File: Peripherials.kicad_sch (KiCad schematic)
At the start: 32 parts, among them J12 USB_C_Receptacle_USB2.0_14P, J13 USB_C_Receptacle_USB2.0_14P, J14 IDC_Cable_02x08, J15 Conn_01x02_Pin, J18 Micro_SD_Card, Q2 NMOS, U12 USBLC6-2P6, U13 USBLC6-2P6, U2 RV-3028-C7

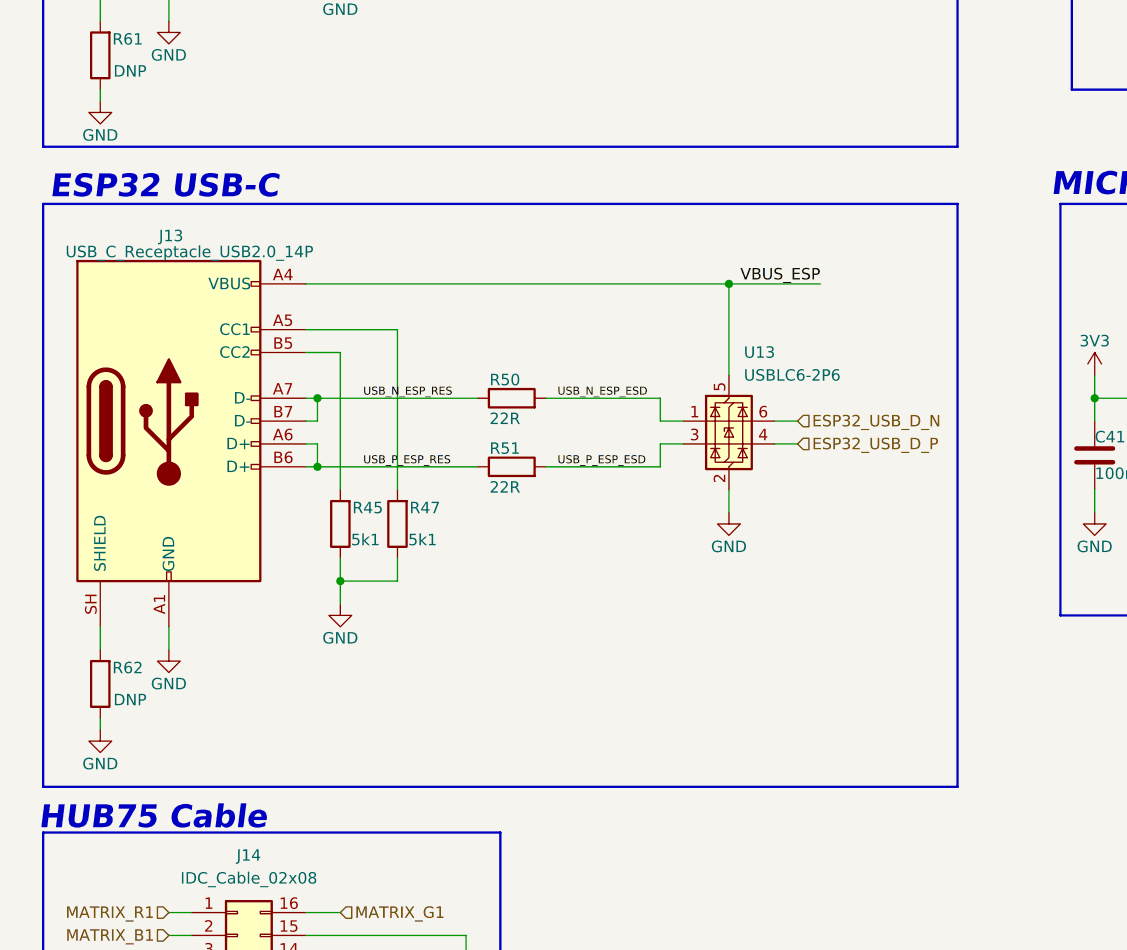
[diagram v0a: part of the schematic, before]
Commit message: got rid of usb
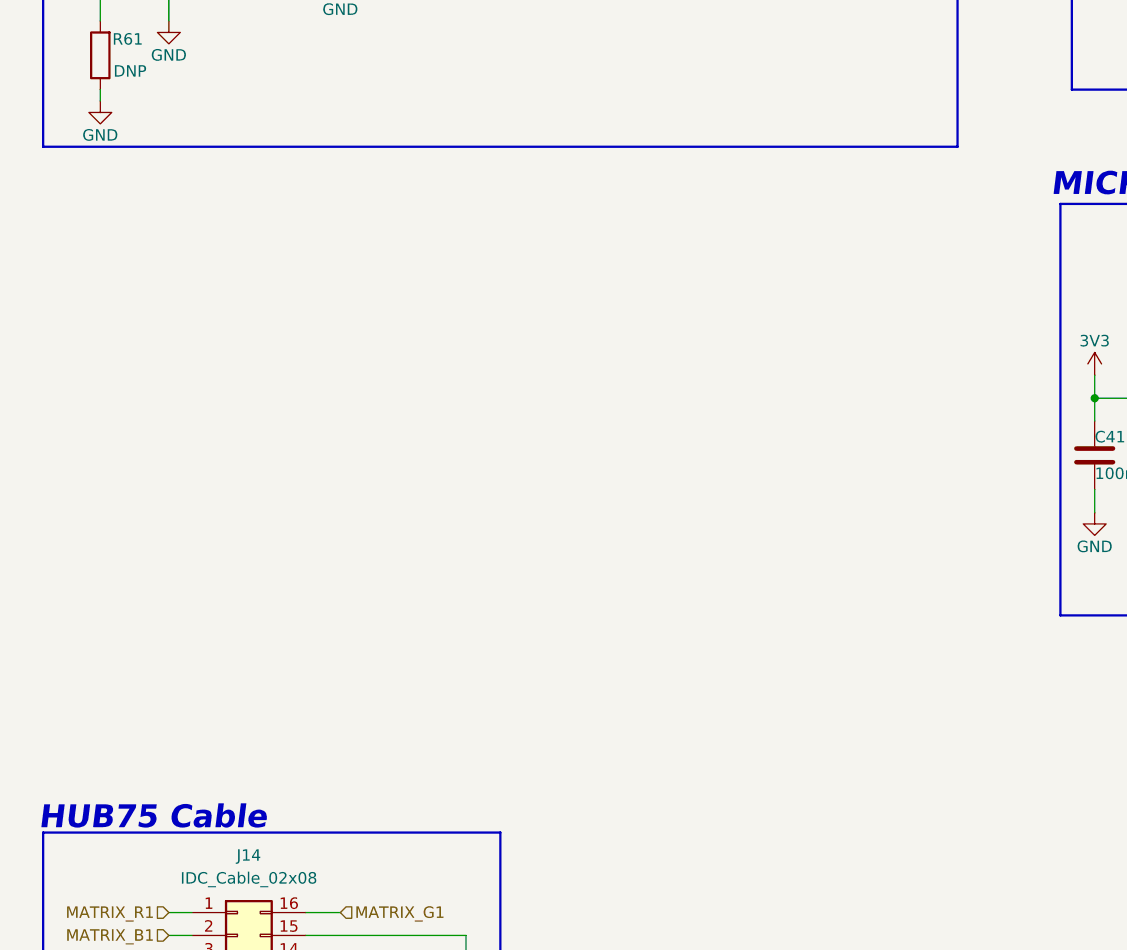
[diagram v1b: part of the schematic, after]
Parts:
- removed J13: USB_C_Receptacle_USB2.0_14P, Connector_USB:USB_C_Receptacle_Palconn_UTC16-G, symbol Connector:USB_C_Receptacle_USB2.0_14P
- removed R45, R47: 5k1, Resistor_SMD:R_0603_1608Metric, symbol Device:R
- removed R50, R51: 22R, Resistor_SMD:R_0603_1608Metric, symbol Device:R
- removed R62: DNP, Resistor_SMD:R_0603_1608Metric, symbol Device:R
- removed U13: USBLC6-2P6, Package_TO_SOT_SMD:SOT-666, symbol Power_Protection:USBLC6-2P6
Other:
- note removed: "ESP32 USB-C"

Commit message: Update Peripherials.kicad_sch
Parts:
- added J1: esp32 left side, symbol Connector_Generic:Conn_01x07
- added J2: esp32 right side, symbol Connector_Generic:Conn_01x07
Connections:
- net 3V3: now also J2.3 (Pin_3)
- net GND: now also J2.2 (Pin_2)
- net I2C3_SCL: now also J1.5 (Pin_5)
- net INT_RTC: now also J2.5 (Pin_5)
- net SPI1_MISO: now also J1.1 (Pin_1)
- net SPI1_MOSI: now also J1.2 (Pin_2)
- net SPI1_SCLK: now also J2.4 (Pin_4)
- net SPI_CS_SD_CARD: now also J1.3 (Pin_3)
- net VBUS_ESP: now also J2.1 (Pin_1)
- new net FAN_PWMD: J1.6 (Pin_6)
- new net ICC3_SDA: J1.4 (Pin_4)
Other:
- note added: "ESP32-C3 MINI headers"
